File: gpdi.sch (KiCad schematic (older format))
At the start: 1 part, among them J6 Audio-Jack-5

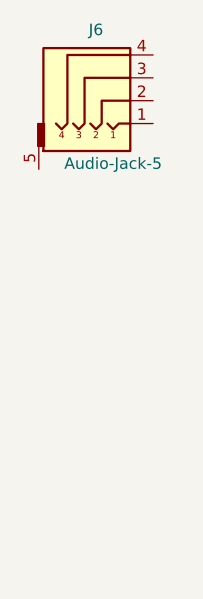
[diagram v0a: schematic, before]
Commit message: micro hdmi connector
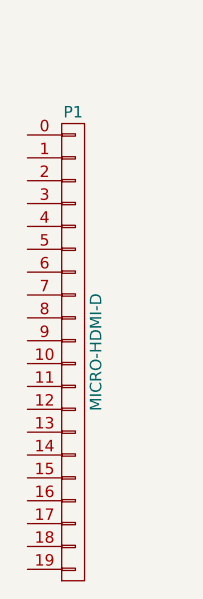
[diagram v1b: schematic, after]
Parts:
- removed J6: Audio-Jack-5, audio-jack:CUI_SJ-43516-SMT, symbol Audio-Jack-5
- added P1: MICRO-HDMI-D, micro-hdmi-d:MICRO-HDMI-D, symbol MICRO-HDMI-D
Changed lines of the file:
@@
 $Descr A4 11693 8268
 encoding utf-8
-Sheet 10 11
+Sheet 11 11
 Title ""
 Date ""
@@
 $EndDescr
 $Comp
-L Audio-Jack-5 J6
-U 1 1 5A133C61
-P 3650 2450
-F 0 "J6" H 3600 2660 50  0000 C CNN
-F 1 "Audio-Jack-5" H 3675 2075 50  0000 C CNN
-F 2 "audio-jack:CUI_SJ-43516-SMT" H 3900 2550 50  0001 C CNN
-F 3 "" H 3900 2550 50  0001 C CNN
-	1    3650 2450
+L MICRO-HDMI-D P1
+U 1 1 5A1343A9
+P 3500 3650
+F 0 "P1" H 3500 4700 50  0000 C CNN
+F 1 "MICRO-HDMI-D" V 3600 3650 50  0000 C CNN
+F 2 "micro-hdmi-d:MICRO-HDMI-D" H 3500 3650 60  0001 C CNN
+F 3 "" H 3500 3650 60  0000 C CNN
+	1    3500 3650
 	1    0    0    -1
 $EndComp
